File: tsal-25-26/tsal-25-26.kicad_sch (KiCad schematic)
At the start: 29 parts, among them J1 043045-0412, Q1 DMP2035U-7, Q3 UJ3N065080K3S, Q4 DMN2056U, Q5 AO3401A, U1 H11L1M, U2 NE555D

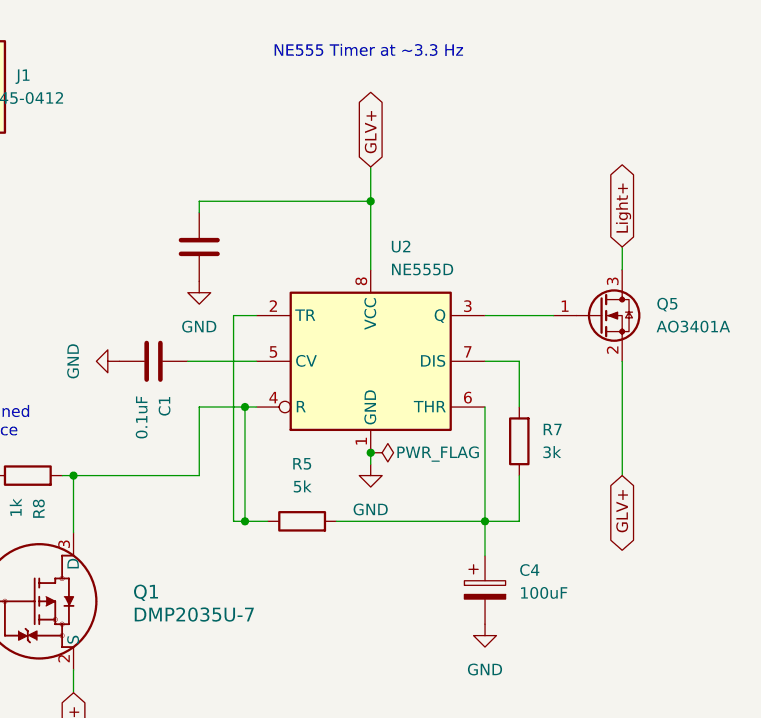
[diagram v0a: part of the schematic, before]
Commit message: new pcb with correct dimensions
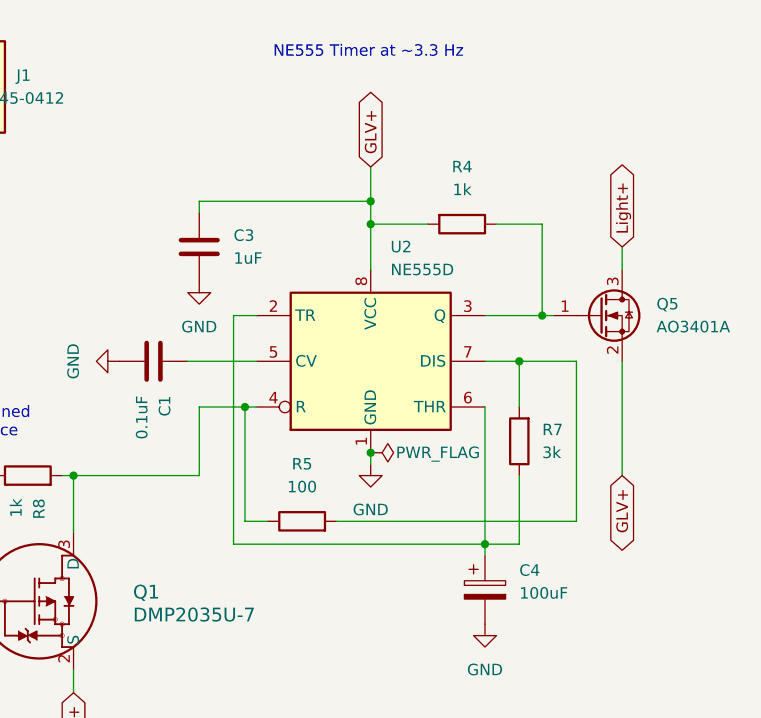
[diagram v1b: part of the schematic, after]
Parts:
- added R4: 1k, Resistor_SMD:R_0805_2012Metric_Pad1.20x1.40mm_HandSolder, symbol Device:R
- H1, H2, H3, H4: footprint MountingHole:MountingHole_4.3mm_M4 -> MountingHole:MountingHole_3.2mm_M3_Pad_TopBottom
- R5: value 5k -> 100
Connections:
- net GLV+: now also R4.2
- net at Q5.1 (G), U2.3 (Q): now also R4.1
- net at Q1.3 (D), R5.1, R8.2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: no longer U2.2 (TR)
- net at C4.1, R7.1, U2.6 (THR): now also U2.2 (TR); no longer R5.2
- net at R7.2, U2.7 (DIS): now also R5.2
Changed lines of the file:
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@@
 	)
 	(junction
-		(at 170.18 77.47)
-		(diameter 0)
-		(color 0 0 0 0)
-	)
-	(junction
 		(at 52.07 116.84)
 		(diameter 0)
@@
 	)
 	(junction
+		(at 157.48 44.45)
+		(diameter 0)
+		(color 0 0 0 0)
+	)
+	(junction
+		(at 170.18 80.01)
+		(diameter 0)
+		(color 0 0 0 0)
+	)
+	(junction
 		(at 102.87 68.58)
 		(diameter 0)
@@
 	)
 	(junction
-		(at 143.51 77.47)
+		(at 176.53 54.61)
 		(diameter 0)
 		(color 0 0 0 0)
@@
 	)
 	(junction
+		(at 173.99 59.69)
+		(diameter 0)
+		(color 0 0 0 0)
+	)
+	(junction
 		(at 43.18 116.84)
 		(diameter 0)
@@
 	(wire
 		(pts
-			(xy 170.18 64.77) (xy 170.18 77.47)
+			(xy 180.34 59.69) (xy 173.99 59.69)
+		)
+		(stroke
+			(width 0)
+			(type default)
+		)
+	)
+	(wire
+		(pts
+			(xy 170.18 64.77) (xy 170.18 80.01)
 		)
 		(stroke
@@
 	(wire
 		(pts
+			(xy 142.24 80.01) (xy 170.18 80.01)
+		)
+		(stroke
+			(width 0)
+			(type default)
+		)
+	)
+	(wire
+		(pts
 			(xy 138.43 41.91) (xy 138.43 43.18)
 		)
@@
 	(wire
 		(pts
+			(xy 176.53 44.45) (xy 176.53 54.61)
+		)
+		(stroke
+			(width 0)
+			(type default)
+		)
+	)
+	(wire
+		(pts
 			(xy 36.83 97.79) (xy 36.83 116.84)
 		)
@@
 	(wire
 		(pts
-			(xy 143.51 77.47) (xy 142.24 77.47)
+			(xy 69.85 88.9) (xy 69.85 99.06)
 		)
 		(stroke
@@
 	(wire
 		(pts
-			(xy 69.85 88.9) (xy 69.85 99.06)
+			(xy 171.45 44.45) (xy 176.53 44.45)
 		)
 		(stroke
@@
 	(wire
 		(pts
-			(xy 69.85 83.82) (xy 78.74 83.82)
+			(xy 173.99 72.39) (xy 173.99 80.01)
 		)
 		(stroke
@@
 	(wire
 		(pts
-			(xy 36.83 52.07) (xy 36.83 80.01)
+			(xy 69.85 83.82) (xy 78.74 83.82)
 		)
 		(stroke
@@
 	(wire
 		(pts
-			(xy 173.99 77.47) (xy 170.18 77.47)
+			(xy 36.83 52.07) (xy 36.83 80.01)
 		)
 		(stroke
@@
 	(wire
 		(pts
+			(xy 180.34 77.47) (xy 180.34 59.69)
+		)
+		(stroke
+			(width 0)
+			(type default)
+		)
+	)
+	(wire
+		(pts
 			(xy 124.46 72.39) (xy 124.46 78.74)
 		)
@@
 	(wire
 		(pts
-			(xy 157.48 41.91) (xy 157.48 49.53)
+			(xy 157.48 41.91) (xy 157.48 44.45)
+		)
+		(stroke
+			(width 0)
+			(type default)
+		)
+	)
+	(wire
+		(pts
+			(xy 170.18 80.01) (xy 170.18 81.28)
 		)
 		(stroke
@@
 	(wire
 		(pts
-			(xy 170.18 54.61) (xy 177.8 54.61)
+			(xy 170.18 54.61) (xy 176.53 54.61)
 		)
 		(stroke
@@
 	(wire
 		(pts
+			(xy 173.99 80.01) (xy 170.18 80.01)
+		)
+		(stroke
+			(width 0)
+			(type default)
+		)
+	)
+	(wire
+		(pts
 			(xy 36.83 116.84) (xy 43.18 116.84)
 		)
@@
 	(wire
 		(pts
+			(xy 157.48 44.45) (xy 157.48 49.53)
+		)
+		(stroke
+			(width 0)
+			(type default)
+		)
+	)
+	(wire
+		(pts
 			(xy 36.83 52.07) (xy 41.91 52.07)
 		)
@@
 	(wire
 		(pts
+			(xy 157.48 44.45) (xy 163.83 44.45)
+		)
+		(stroke
+			(width 0)
+			(type default)
+		)
+	)
+	(wire
+		(pts
 			(xy 86.36 68.58) (xy 102.87 68.58)
 		)
@@
 	(wire
 		(pts
-			(xy 142.24 77.47) (xy 142.24 54.61)
+			(xy 142.24 54.61) (xy 142.24 80.01)
 		)
 		(stroke
@@
 	(wire
 		(pts
-			(xy 43.18 104.14) (xy 43.18 106.68)
+			(xy 153.67 77.47) (xy 180.34 77.47)
 		)
 		(stroke
@@
 	(wire
 		(pts
-			(xy 102.87 63.5) (xy 102.87 68.58)
+			(xy 43.18 104.14) (xy 43.18 106.68)
 		)
 		(stroke
@@
 	(wire
 		(pts
-			(xy 52.07 116.84) (xy 52.07 114.3)
+			(xy 102.87 63.5) (xy 102.87 68.58)
 		)
 		(stroke
@@
 	(wire
 		(pts
-			(xy 52.07 104.14) (xy 62.23 104.14)
+			(xy 52.07 116.84) (xy 52.07 114.3)
 		)
 		(stroke
@@
 	(wire
 		(pts
-			(xy 146.05 77.47) (xy 143.51 77.47)
+			(xy 52.07 104.14) (xy 62.23 104.14)
 		)
 		(stroke
@@
 	(wire
 		(pts
-			(xy 52.07 104.14) (xy 52.07 106.68)
+			(xy 146.05 77.47) (xy 143.51 77.47)
 		)
 		(stroke
@@
 	(wire
 		(pts
-			(xy 173.99 72.39) (xy 173.99 77.47)
+			(xy 52.07 104.14) (xy 52.07 106.68)
 		)
 		(stroke
@@
 	(wire
 		(pts
-			(xy 170.18 77.47) (xy 153.67 77.47)
+			(xy 52.07 66.04) (xy 52.07 67.31)
 		)
 		(stroke
@@
 	(wire
 		(pts
-			(xy 52.07 66.04) (xy 52.07 67.31)
+			(xy 170.18 59.69) (xy 173.99 59.69)
 		)
 		(stroke
@@
 	(wire
 		(pts
-			(xy 170.18 59.69) (xy 173.99 59.69)
+			(xy 176.53 54.61) (xy 177.8 54.61)
 		)
 		(stroke
@@
 	(wire
 		(pts
-			(xy 170.18 77.47) (xy 170.18 81.28)
-		)
-		(stroke
-			(width 0)
-			(type default)
-		)
-	)
-	(wire
-		(pts
 			(xy 59.69 68.58) (xy 62.23 68.58)
 		)
@@
 			)
 		)
-		(property "Value" "5k"
+		(property "Value" "100"
 			(at 149.86 73.66 90)
 			(effects
@@
 				)
 				(justify right)
-				(hide yes)
 			)
 		)
@@
 				)
 				(justify right)
-				(hide yes)
 			)
 		)
@@
 			)
 		)
-		(property "Footprint" "MountingHole:MountingHole_4.3mm_M4"
+		(property "Footprint" "MountingHole:MountingHole_3.2mm_M3_Pad_TopBottom"
 			(at 19.05 24.13 0)
 			(effects
@@
 			)
 		)
-		(property "Footprint" "MountingHole:MountingHole_4.3mm_M4"
+		(property "Footprint" "MountingHole:MountingHole_3.2mm_M3_Pad_TopBottom"
 			(at 19.05 34.29 0)
 			(effects
@@
 			)
 		)
-		(property "Footprint" "MountingHole:MountingHole_4.3mm_M4"
+		(property "Footprint" "MountingHole:MountingHole_3.2mm_M3_Pad_TopBottom"
 			(at 19.05 39.37 0)
 			(effects
@@
 	)
 	(symbol
+		(lib_id "Device:R")
+		(at 167.64 44.45 270)
+		(unit 1)
+		(exclude_from_sim no)
+		(in_bom yes)
+		(on_board yes)
+		(dnp no)
+		(fields_autoplaced yes)
+		(property "Reference" "R4"
+			(at 167.64 38.1 90)
+			(effects
+				(font
+					(size 1.27 1.27)
+				)
+			)
+		)
+		(property "Value" "1k"
+			(at 167.64 40.64 90)
+			(effects
+				(font
+					(size 1.27 1.27)
+				)
+			)
+		)
+		(property "Footprint" "Resistor_SMD:R_0805_2012Metric_Pad1.20x1.40mm_HandSolder"
+			(at 167.64 42.672 90)
+			(effects
+				(font
+					(size 1.27 1.27)
+				)
+				(hide yes)
+			)
+		)
+		(property "Datasheet" "~"
+			(at 167.64 44.45 0)
+			(effects
+				(font
+					(size 1.27 1.27)
+				)
+				(hide yes)
+			)
+		)
+		(property "Description" "Resistor"
+			(at 167.64 44.45 0)
+			(effects
+				(font
+					(size 1.27 1.27)
+				)
+				(hide yes)
+			)
+		)
+		(pin "2"
+		)
+		(pin "1"
+		)
+		(instances
+			(project "tsal-25-26"
+				(path "/d0262e13-a8ab-42db-962e-1ef7dd9c8d4a"
+					(reference "R4")
+					(unit 1)
+				)
+			)
+		)
+	)
+	(symbol
 		(lib_id "Diode:BZT52Bxx")
 		(at 52.07 62.23 270)
@@
 			)
 		)
-		(property "Footprint" "MountingHole:MountingHole_4.3mm_M4"
+		(property "Footprint" "MountingHole:MountingHole_3.2mm_M3_Pad_TopBottom"
 			(at 19.05 29.21 0)
 			(effects
